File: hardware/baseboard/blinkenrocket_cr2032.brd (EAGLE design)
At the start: 96.3 x 47 mm, 22 parts, among them SW1 SWITCH-4POMRON-6-6-SWITCH, SW2 SWITCH-4POMRON-6-6-SWITCH, U2 EEPROM-I2CEIAJ

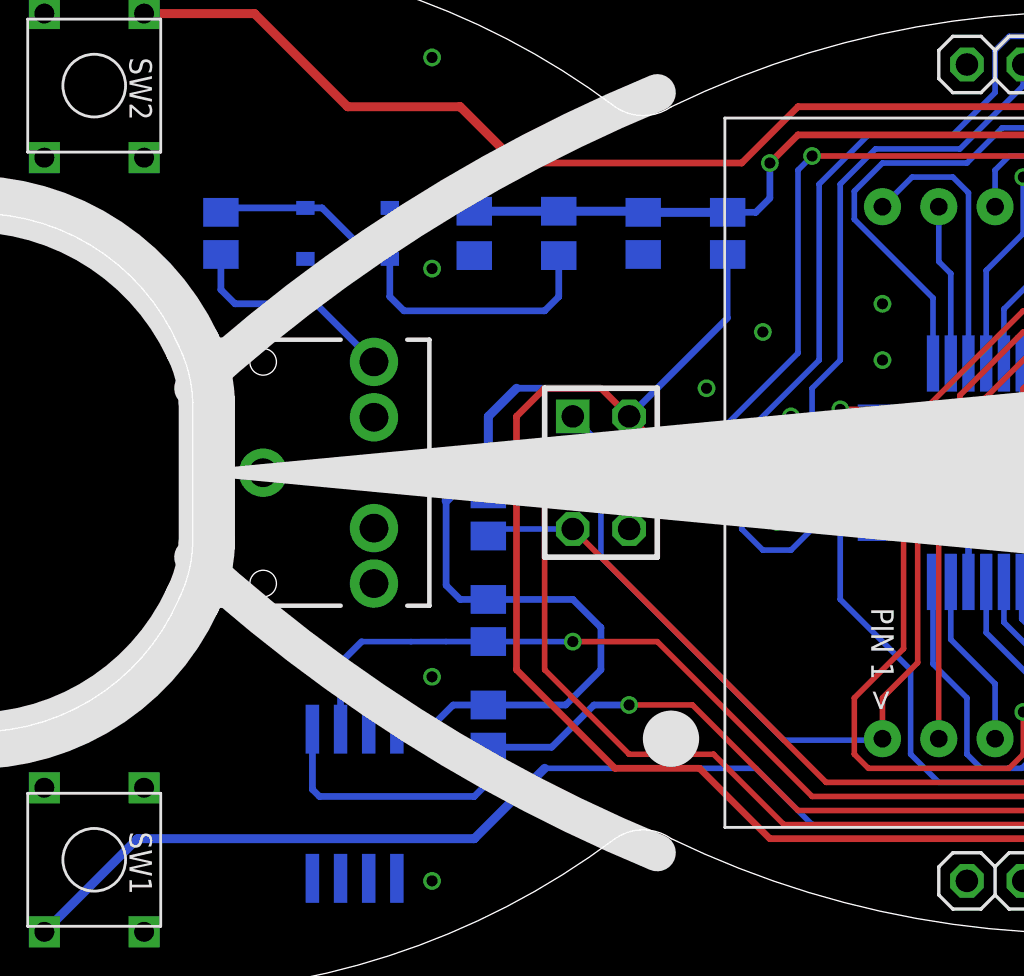
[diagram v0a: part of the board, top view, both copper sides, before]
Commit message: 1206 instead of 0805 - this is easier to solder actually...
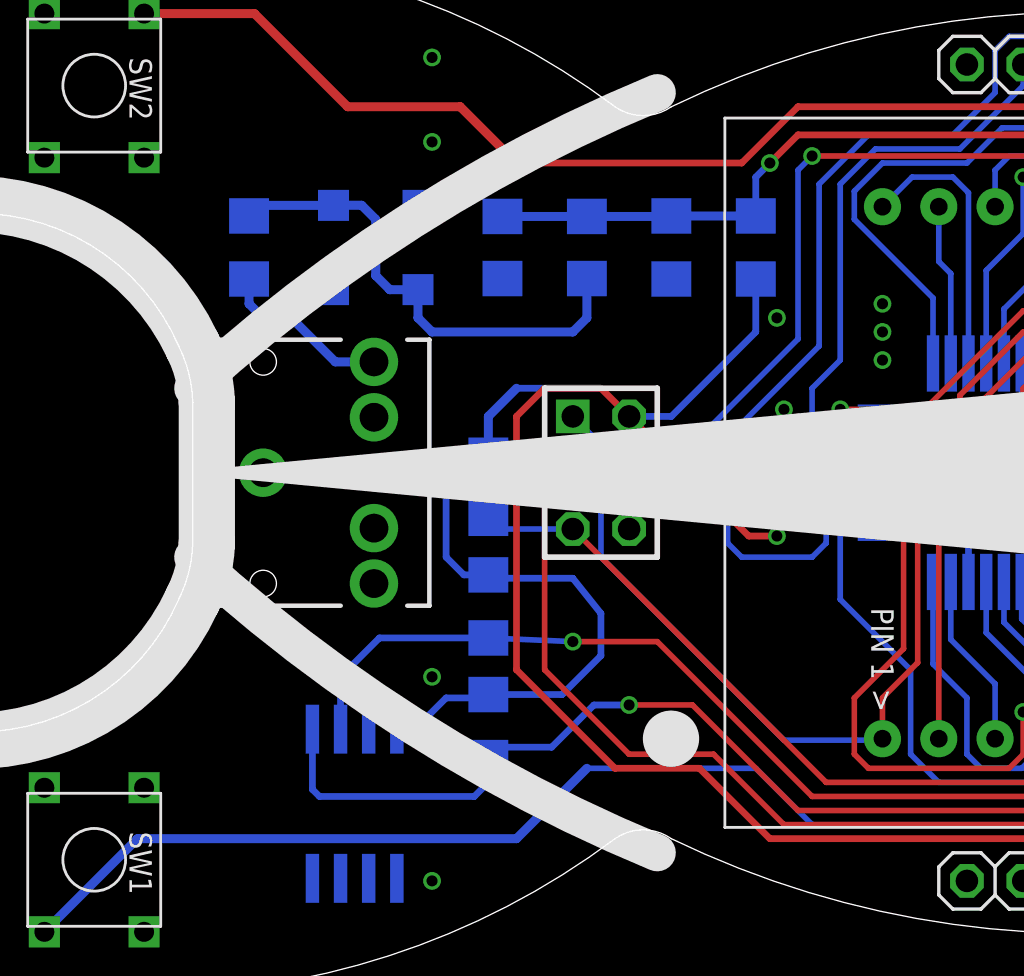
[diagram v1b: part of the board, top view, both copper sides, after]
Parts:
- C1, C2, C3: device resistor:C0805K -> resistor:C1206
- D1, D2: device SparkFun-DiscreteSemi:SOD-323 -> diode-1:SOD123
- R1, R2, R3, R4, R5, R6: device resistor:M0805 -> resistor:R1206
- moved R2 1.42 mm to (42.5, 35.6)
- moved D1 1.42 mm to (31.1, 35.6)
- moved D2 1.42 mm to (27.3, 35.6)
- moved R3 1.42 mm to (23.5, 35.6)
- moved C1 1.42 mm to (38.7, 35.6)
- moved C2 1.42 mm to (34.9, 35.6)
- moved R1 1.42 mm to (46.4, 35.6)
- moved R6 1.27 mm to (34.3, 24.8)
- moved R5 0.63 mm to (34.3, 19.4)
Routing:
- net AVR_AUDIO_IN: track 68.6 -> 65.4 mm
- net GND: track 7.33 -> 4.30 mm
- net E5: track 41.0 -> 43.1 mm
- net N$3: track 20.4 -> 22.1 mm
- net N$1: track 9.84 -> 8.32 mm
